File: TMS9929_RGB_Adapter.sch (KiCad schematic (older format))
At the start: 73 parts, among them P1 CONN_01X06, P10 12V, P2 CONN_01X08, P3 SEL, P4 SEL, P5 SEL, P6 CONN_01X01, P7 CONN_01X01, P8 CONN_01X01, P9 CONN_01X01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

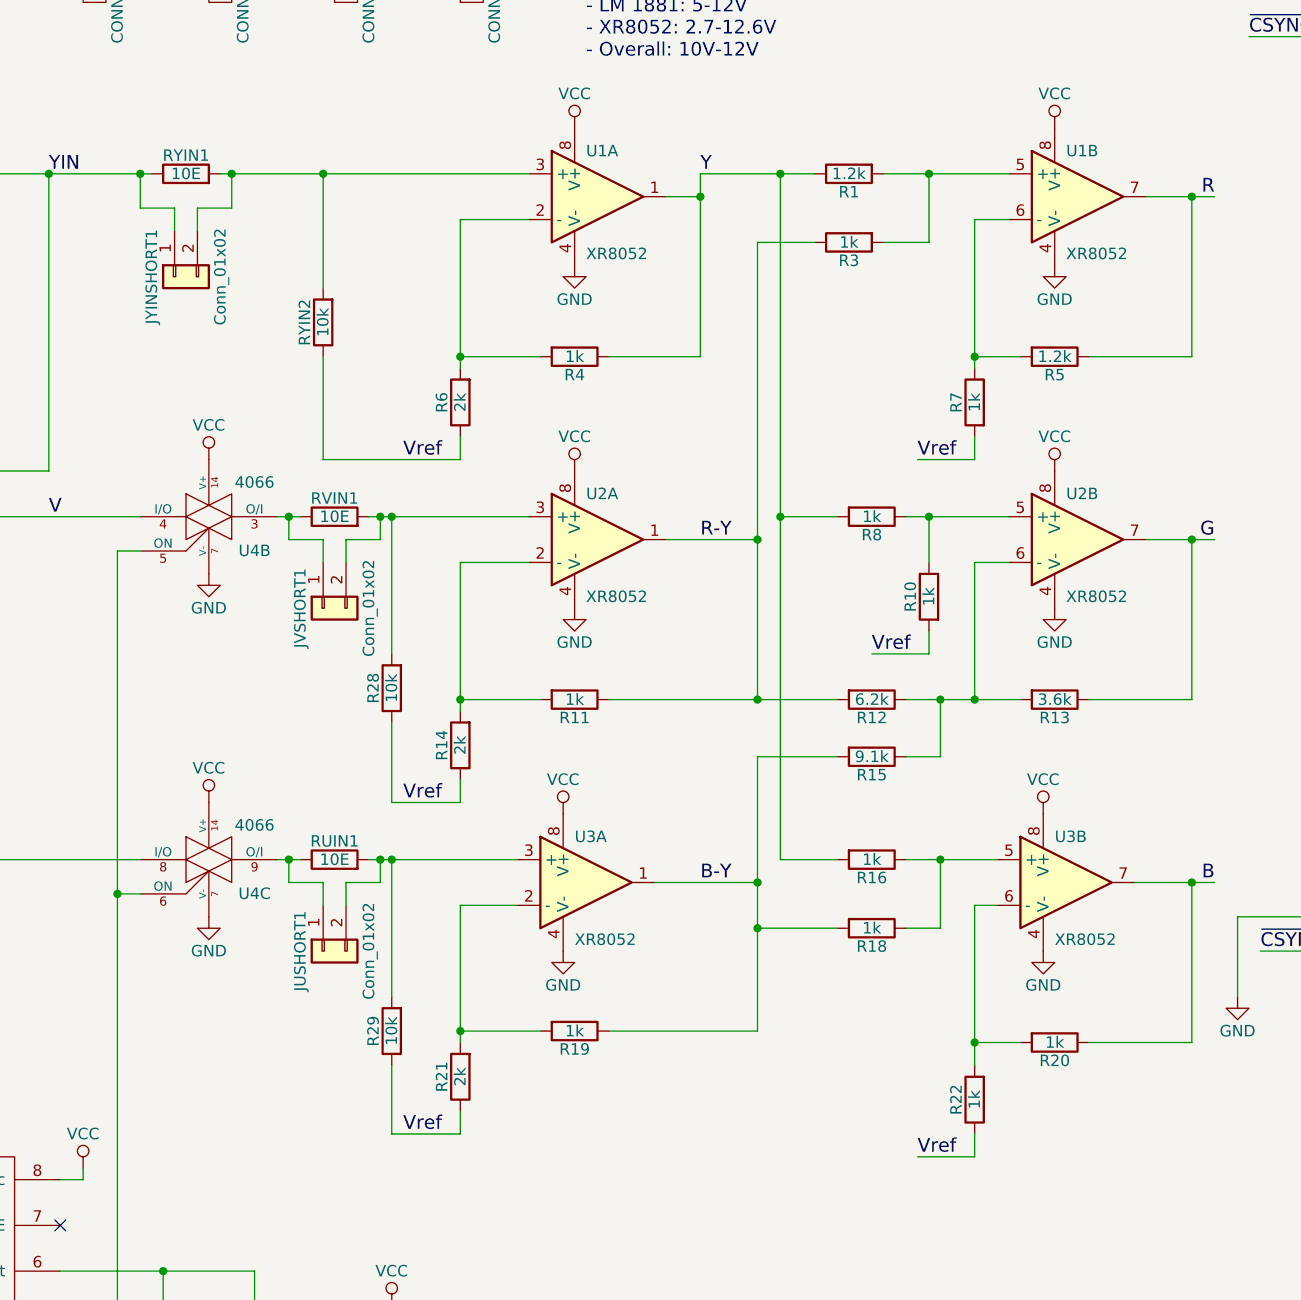
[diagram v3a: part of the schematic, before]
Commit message: Added new resistors in parallel to existing ones to solder standard resistor values
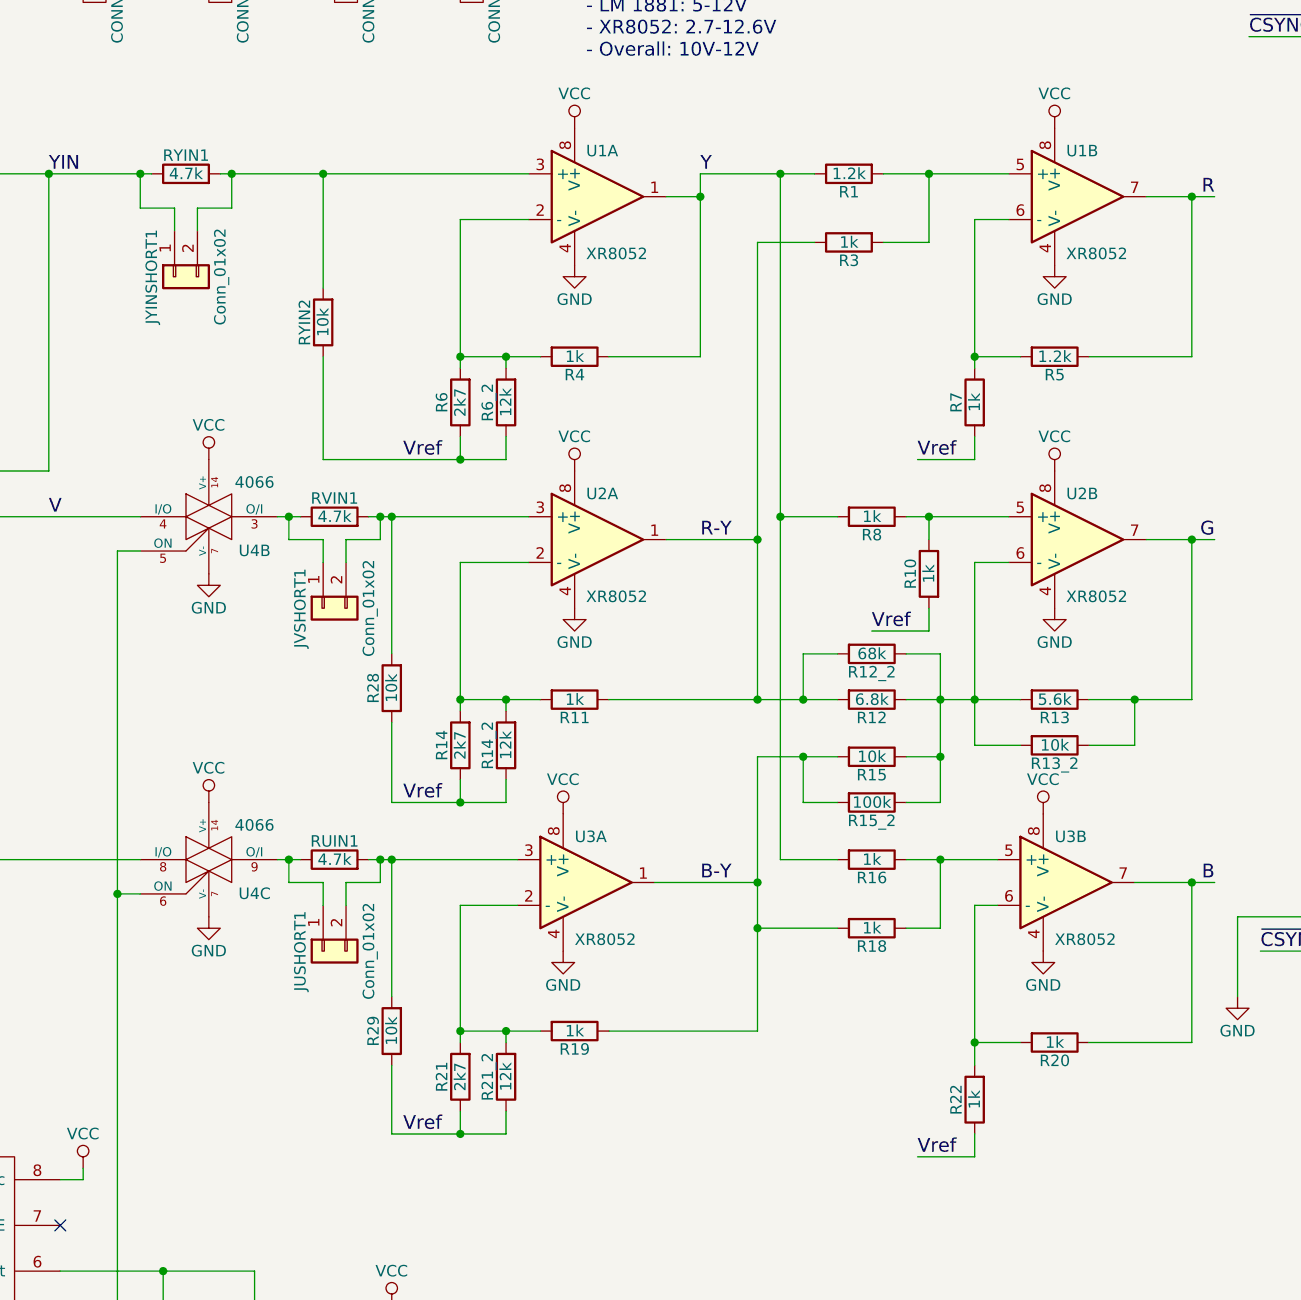
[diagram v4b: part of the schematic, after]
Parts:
- added R12_2: 68k, Resistors_SMD:R_0805_HandSoldering, symbol R
- added R13_2: 10k, Resistors_SMD:R_0805_HandSoldering, symbol R
- added R14_2, R21_2, R6_2: 12k, Resistors_SMD:R_0805_HandSoldering, symbol R
- added R15_2: 100k, Resistors_SMD:R_0805_HandSoldering, symbol R
- R12: value 6.2k -> 6.8k
- R13: value 3.6k -> 5.6k
- R14, R21, R6: value 2k -> 2k7
- R15: value 9.1k -> 10k
- RUIN1, RVIN1, RYIN1: value 10E -> 4.7k
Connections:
- net B-Y: now also R15_2.2
- net G: now also R13_2.1
- net R-Y: now also R12_2.2
- net Vref: now also R14_2.1, R21_2.1, R6_2.1
- net at R11.2, R14.2, U2.2 (-): now also R14_2.2
- net at R12.1, R13.2, R15.1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: now also R12_2.1, R13_2.2, R15_2.1
- net at R19.2, R21.2, U3.2 (-): now also R21_2.2
- net at R4.2, R6.2, U1.2 (-): now also R6_2.2
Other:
- moved on the sheet: R10
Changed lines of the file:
@@
 P 4500 4150
 F 0 "R14" V 4580 4150 50  0000 C CNN
-F 1 "2k" V 4500 4150 50  0000 C CNN
+F 1 "2k7" V 4500 4150 50  0000 C CNN
 F 2 "Resistors_SMD:R_0805_HandSoldering" V 4430 4150 50  0001 C CNN
 F 3 "" H 4500 4150 50  0000 C CNN
@@
 P 7100 3950
 F 0 "R13" V 7180 3950 50  0000 C CNN
-F 1 "3.6k" V 7100 3950 50  0000 C CNN
+F 1 "5.6k" V 7100 3950 50  0000 C CNN
 F 2 "Resistors_SMD:R_0805_HandSoldering" V 7030 3950 50  0001 C CNN
 F 3 "" H 7100 3950 50  0000 C CNN
@@
 P 4500 5600
 F 0 "R21" V 4580 5600 50  0000 C CNN
-F 1 "2k" V 4500 5600 50  0000 C CNN
+F 1 "2k7" V 4500 5600 50  0000 C CNN
 F 2 "Resistors_SMD:R_0805_HandSoldering" V 4430 5600 50  0001 C CNN
 F 3 "" H 4500 5600 50  0000 C CNN
@@
 P 4500 2650
 F 0 "R6" V 4580 2650 50  0000 C CNN
-F 1 "2k" V 4500 2650 50  0000 C CNN
+F 1 "2k7" V 4500 2650 50  0000 C CNN
 F 2 "Resistors_SMD:R_0805_HandSoldering" V 4430 2650 50  0001 C CNN
 F 3 "" H 4500 2650 50  0000 C CNN
@@
 P 6300 3950
 F 0 "R12" V 6380 3950 50  0000 C CNN
-F 1 "6.2k" V 6300 3950 50  0000 C CNN
+F 1 "6.8k" V 6300 3950 50  0000 C CNN
 F 2 "Resistors_SMD:R_0805_HandSoldering" V 6230 3950 50  0001 C CNN
 F 3 "" H 6300 3950 50  0000 C CNN
@@
 P 6300 4200
 F 0 "R15" V 6380 4200 50  0000 C CNN
-F 1 "9.1k" V 6300 4200 50  0000 C CNN
+F 1 "10k" V 6300 4200 50  0000 C CNN
 F 2 "Resistors_SMD:R_0805_HandSoldering" V 6230 4200 50  0001 C CNN
 F 3 "" H 6300 4200 50  0000 C CNN
@@
 L R R10
 U 1 1 5766A98B
-P 6550 3500
-F 0 "R10" V 6630 3500 50  0000 C CNN
-F 1 "1k" V 6550 3500 50  0000 C CNN
-F 2 "Resistors_SMD:R_0805_HandSoldering" V 6480 3500 50  0001 C CNN
-F 3 "" H 6550 3500 50  0000 C CNN
-	1    6550 3500
+P 6550 3400
+F 0 "R10" V 6630 3400 50  0000 C CNN
+F 1 "1k" V 6550 3400 50  0000 C CNN
+F 2 "Resistors_SMD:R_0805_HandSoldering" V 6480 3400 50  0001 C CNN
+F 3 "" H 6550 3400 50  0000 C CNN
+	1    6550 3400
 	-1   0    0    -1
 $EndComp
@@
 Text Label 4250 4400 0    60   ~ 0
 Vref
-Text Label 6300 3750 0    60   ~ 0
+Text Label 6300 3650 0    60   ~ 0
 Vref
 Text Label 4250 2900 0    60   ~ 0
@@
 	9500 4750 9250 4750
 Wire Wire Line
-	4200 5850 4500 5850
+	4200 5850 4700 5850
 Wire Wire Line
 	4500 5850 4500 5750
@@
 	6750 5850 6750 5950
 Wire Wire Line
-	6550 3750 6300 3750
-Wire Wire Line
-	6550 3650 6550 3750
-Wire Wire Line
-	4200 4400 4500 4400
+	6550 3650 6300 3650
+Wire Wire Line
+	6550 3550 6550 3650
+Wire Wire Line
+	4200 4400 4700 4400
 Wire Wire Line
 	4500 4400 4500 4300
@@
 	4500 2900 4500 2800
 Wire Wire Line
-	3900 2900 4500 2900
+	3900 2900 4700 2900
 Wire Wire Line
 	6750 2900 6500 2900
@@
 Connection ~ 6550 3150
 Wire Wire Line
-	6550 3350 6550 3150
+	6550 3250 6550 3150
 Wire Wire Line
 	6450 3150 6900 3150
@@
 Connection ~ 6600 3950
 Wire Wire Line
-	6600 4200 6600 3950
+	6600 3750 6600 4400
 Connection ~ 5800 4750
 Wire Wire Line
-	6150 4200 5800 4200
+	5800 4200 6150 4200
 Connection ~ 6750 3950
 Connection ~ 5800 3950
@@
 	5550 1650 6050 1650
 Wire Wire Line
-	6750 3950 6750 3350
+	6750 3350 6750 4150
 Connection ~ 6750 5450
 Wire Wire Line
@@
 Connection ~ 4500 2450
 Wire Wire Line
-	4850 2450 4500 2450
+	4500 2450 4850 2450
 Wire Wire Line
 	4500 1850 4500 2500
@@
 	4500 4850 4500 5450
 Wire Wire Line
-	4850 5400 4500 5400
+	4500 5400 4850 5400
 Wire Wire Line
 	7500 3250 7800 3250
@@
 	4500 3350 4500 4000
 Wire Wire Line
-	4850 3950 4500 3950
+	4500 3950 4850 3950
 Wire Wire Line
 	5800 3250 5400 3250
@@
 P 3300 1650
 F 0 "RYIN1" V 3380 1650 50  0000 C CNN
-F 1 "10E" V 3300 1650 50  0000 C CNN
+F 1 "4.7k" V 3300 1650 50  0000 C CNN
 F 2 "Resistors_SMD:R_0805_HandSoldering" V 3230 1650 50  0001 C CNN
 F 3 "" H 3300 1650 50  0000 C CNN
@@
 P 3950 3150
 F 0 "RVIN1" V 4030 3150 50  0000 C CNN
-F 1 "10E" V 3950 3150 50  0000 C CNN
+F 1 "4.7k" V 3950 3150 50  0000 C CNN
 F 2 "Resistors_SMD:R_0805_HandSoldering" V 3880 3150 50  0001 C CNN
 F 3 "" H 3950 3150 50  0000 C CNN
@@
 P 3950 4650
 F 0 "RUIN1" V 4030 4650 50  0000 C CNN
-F 1 "10E" V 3950 4650 50  0000 C CNN
+F 1 "4.7k" V 3950 4650 50  0000 C CNN
 F 2 "Resistors_SMD:R_0805_HandSoldering" V 3880 4650 50  0001 C CNN
 F 3 "" H 3950 4650 50  0000 C CNN
@@
 Text Notes 5050 1150 0    60   ~ 0
 Supply voltages:\n- TL081: +/-5V to +/-15V => 10V-30V\n- HEF 4066: 3-15V\n- LM 1881: 5-12V\n- XR8052: 2.7-12.6V\n- Overall: 10V-12V\n
+$Comp
+L R R14_2
+U 1 1 59C841B4
+P 4700 4150
+F 0 "R14_2" V 4780 4150 50  0000 C CNN
+F 1 "12k" V 4700 4150 50  0000 C CNN
+F 2 "Resistors_SMD:R_0805_HandSoldering" V 4630 4150 50  0001 C CNN
+F 3 "" H 4700 4150 50  0000 C CNN
+	1    4700 4150
+	-1   0    0    1
+$EndComp
+Wire Wire Line
+	4700 4400 4700 4300
+Connection ~ 4500 4400
+Wire Wire Line
+	4700 4000 4700 3950
+Connection ~ 4700 3950
+$Comp
+L R R21_2
+U 1 1 59C8476E
+P 4700 5600
+F 0 "R21_2" V 4780 5600 50  0000 C CNN
+F 1 "12k" V 4700 5600 50  0000 C CNN
+F 2 "Resistors_SMD:R_0805_HandSoldering" V 4630 5600 50  0001 C CNN
+F 3 "" H 4700 5600 50  0000 C CNN
+	1    4700 5600
+	-1   0    0    1
+$EndComp
+Wire Wire Line
+	4700 5850 4700 5750
+Connection ~ 4500 5850
+Wire Wire Line
+	4700 5450 4700 5400
+Connection ~ 4700 5400
+$Comp
+L R R6_2
+U 1 1 59C850AE
+P 4700 2650
+F 0 "R6_2" V 4780 2650 50  0000 C CNN
+F 1 "12k" V 4700 2650 50  0000 C CNN
+F 2 "Resistors_SMD:R_0805_HandSoldering" V 4630 2650 50  0001 C CNN
+F 3 "" H 4700 2650 50  0000 C CNN
+	1    4700 2650
+	-1   0    0    1
+$EndComp
+Wire Wire Line
+	4700 2900 4700 2800
+Connection ~ 4500 2900
+Wire Wire Line
+	4700 2500 4700 2450
+Connection ~ 4700 2450
+$Comp
+L R R15_2
+U 1 1 59C85B57
+P 6300 4400
+F 0 "R15_2" V 6380 4400 50  0000 C CNN
+F 1 "100k" V 6300 4400 50  0000 C CNN
+F 2 "Resistors_SMD:R_0805_HandSoldering" V 6230 4400 50  0001 C CNN
+F 3 "" H 6300 4400 50  0000 C CNN
+	1    6300 4400
+	0    1    1    0
+$EndComp
+Wire Wire Line
+	6600 4400 6450 4400
+Connection ~ 6600 4200
+Wire Wire Line
+	6150 4400 6000 4400
+Wire Wire Line
+	6000 4400 6000 4200
+Connection ~ 6000 4200
+$Comp
+L R R13_2
+U 1 1 59C86052
+P 7100 4150
+F 0 "R13_2" V 7180 4150 50  0000 C CNN
+F 1 "10k" V 7100 4150 50  0000 C CNN
+F 2 "Resistors_SMD:R_0805_HandSoldering" V 7030 4150 50  0001 C CNN
+F 3 "" H 7100 4150 50  0000 C CNN
+	1    7100 4150
+	0    1    1    0
+$EndComp
+Wire Wire Line
+	7250 4150 7450 4150
+Wire Wire Line
+	7450 4150 7450 3950
+Connection ~ 7450 3950
+Wire Wire Line
+	6750 4150 6950 4150
+$Comp
+L R R12_2
+U 1 1 59C86A03
+P 6300 3750
+F 0 "R12_2" V 6380 3750 50  0000 C CNN
+F 1 "68k" V 6300 3750 50  0000 C CNN
+F 2 "Resistors_SMD:R_0805_HandSoldering" V 6230 3750 50  0001 C CNN
+F 3 "" H 6300 3750 50  0000 C CNN
+	1    6300 3750
+	0    1    1    0
+$EndComp
+Wire Wire Line
+	6600 3750 6450 3750
+Wire Wire Line
+	6150 3750 6000 3750
+Wire Wire Line
+	6000 3750 6000 3950
+Connection ~ 6000 3950
 $EndSCHEMATC
